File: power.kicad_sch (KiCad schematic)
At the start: 20 parts, among them IC3 CH224K, J5 USB_C_Receptacle_USB2.0, J6 Barrel_Jack, U13 TPD2EUSB30, U20 TPS5430DDA, U9 AMS1117-3.3

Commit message: Fix ERC warnings
See #28
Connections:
- no-connect marks 6 -> 7
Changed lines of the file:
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@@
+	)
+	(junction
+		(at 62.23 27.94)
+		(diameter 0)
+		(color 0 0 0 0)
 	)
 	(junction
@@
 	)
 	(no_connect
+		(at 151.13 35.56)
+	)
+	(no_connect
 		(at 40.64 173.99)
 	)
@@
 	(wire
 		(pts
+			(xy 54.61 25.4) (xy 54.61 27.94)
+		)
+		(stroke
+			(width 0)
+			(type default)
+		)
+	)
+	(wire
+		(pts
 			(xy 36.83 127) (xy 45.72 127)
 		)
@@
 	(wire
 		(pts
-			(xy 62.23 25.4) (xy 62.23 33.02)
+			(xy 62.23 25.4) (xy 62.23 27.94)
 		)
 		(stroke
@@
 	(wire
 		(pts
+			(xy 62.23 27.94) (xy 62.23 33.02)
+		)
+		(stroke
+			(width 0)
+			(type default)
+		)
+	)
+	(wire
+		(pts
 			(xy 77.47 168.91) (xy 83.82 168.91)
+		)
+		(stroke
+			(width 0)
+			(type default)
+		)
+	)
+	(wire
+		(pts
+			(xy 54.61 27.94) (xy 62.23 27.94)
 		)
 		(stroke
@@
 					(unit 1)
 				)
+			)
+		)
+	)
+	(symbol
+		(lib_id "power:PWR_FLAG")
+		(at 54.61 25.4 0)
+		(unit 1)
+		(exclude_from_sim no)
+		(in_bom yes)
+		(on_board yes)
+		(dnp no)
+		(fields_autoplaced yes)
+		(property "Reference" "#FLG09"
+			(at 54.61 23.495 0)
+			(effects
+				(font
+					(size 1.27 1.27)
+				)
+				(hide yes)
+			)
+		)
+		(property "Value" "PWR_FLAG"
+			(at 54.61 20.32 0)
+			(effects
+				(font
+					(size 1.27 1.27)
+				)
+			)
+		)
+		(property "Footprint" ""
+			(at 54.61 25.4 0)
+			(effects
+				(font
+					(size 1.27 1.27)
+				)
+				(hide yes)
+			)
+		)
+		(property "Datasheet" "~"
+			(at 54.61 25.4 0)
+			(effects
+				(font
+					(size 1.27 1.27)
+				)
+				(hide yes)
+			)
+		)
+		(property "Description" "Special symbol for telling ERC where power comes from"
+			(at 54.61 25.4 0)
+			(effects
+				(font
+					(size 1.27 1.27)
+				)
+				(hide yes)
+			)
+		)
+		(pin "1"
+		)
+		(instances
+			(project ""
+				(path "/b3c8a28b-9ce1-4002-b8e8-ef8cb73fe031/673a8a36-5ad4-4c13-9f11-024cf0bef494"
+					(reference "#FLG09")
+					(unit 1)
+				)

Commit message: Add missing rotation offset attribute
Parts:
- C39: JLCPCB Rotation Offset (none) -> 180
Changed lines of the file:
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@@
 			)
 		)
-		(property "LCSC alt" ""
+		(property "JLCPCB Rotation Offset" "180"
 			(at 97.79 172.72 0)
 			(effects

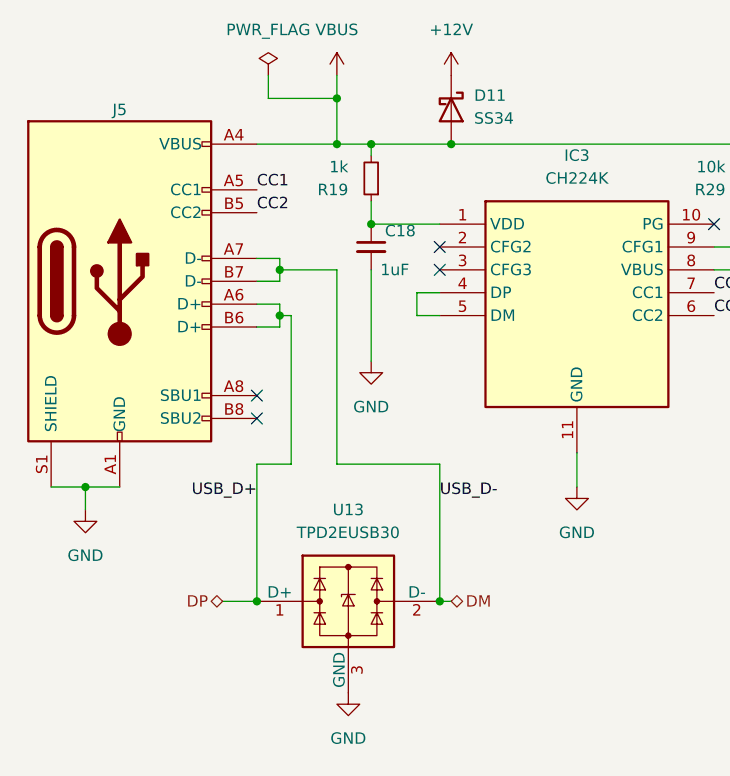
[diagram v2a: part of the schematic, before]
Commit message: Fix ERC errors
Closes #28
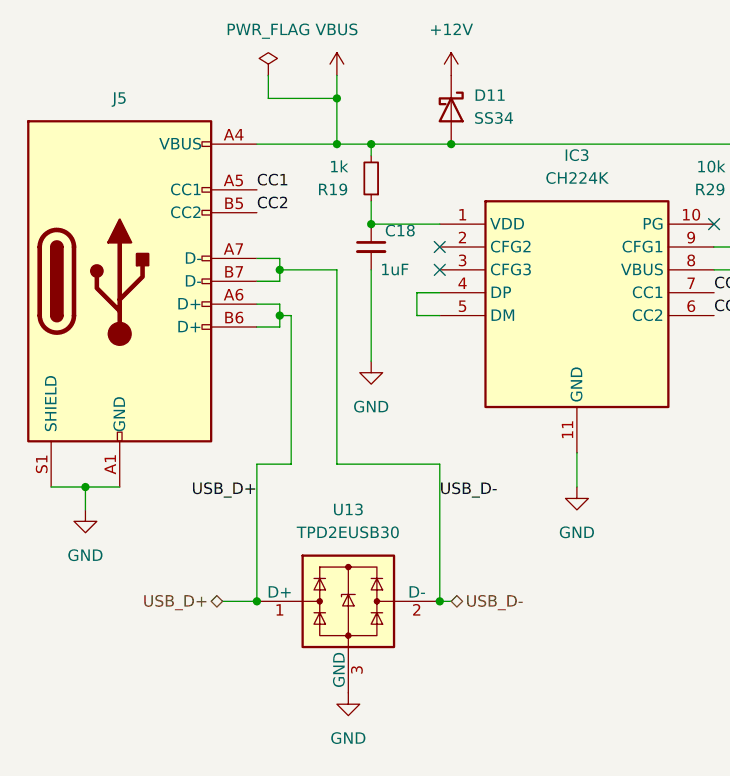
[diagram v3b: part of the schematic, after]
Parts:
- J5: symbol Connector:USB_C_Receptacle_USB2.0 -> Connector:USB_C_Receptacle_USB2.0_14P
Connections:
- net DM renamed USB_D-
- net DP renamed USB_D+
- no-connect marks 7 -> 5
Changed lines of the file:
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@@
 	)
 	(no_connect
-		(at 53.34 60.96)
-	)
-	(no_connect
 		(at 151.13 35.56)
 	)
@@
 	)
 	(no_connect
-		(at 53.34 63.5)
-	)
-	(no_connect
 		(at 73.66 46.99)
 	)
@@
 		)
 	)
-	(hierarchical_label "DM"
+	(hierarchical_label "USB_D-"
 		(shape bidirectional)
 		(at 74.93 83.82 0)
@@
 		)
 	)
-	(hierarchical_label "DP"
+	(hierarchical_label "USB_D+"
 		(shape bidirectional)
 		(at 49.53 83.82 180)
@@
 	)
 	(symbol
-		(lib_id "Connector:USB_C_Receptacle_USB2.0")
+		(lib_id "Connector:USB_C_Receptacle_USB2.0_14P")
 		(at 38.1 48.26 0)
 		(unit 1)
@@
 		(fields_autoplaced yes)
 		(property "Reference" "J5"
-			(at 38.1 29.21 0)
+			(at 38.1 27.94 0)
 			(effects
 				(font
@@
 		(pin "A7"
 		)
-		(pin "A8"
-		)
 		(pin "A9"
 		)
@@
 		(pin "B7"
 		)
-		(pin "B8"
-		)
 		(pin "B9"

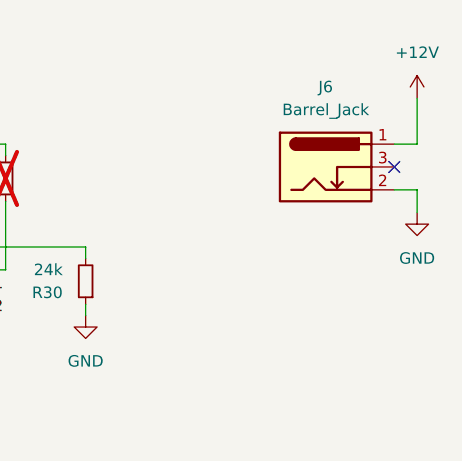
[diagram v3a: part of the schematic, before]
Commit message: Connect GND on DC barrel jack
Closes #35
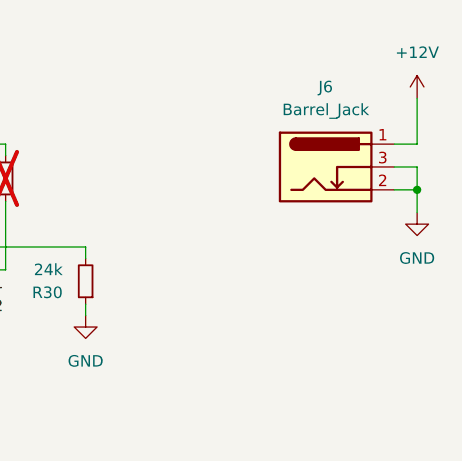
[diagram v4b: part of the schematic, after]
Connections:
- net GND: now also J6.3
- no-connect marks 5 -> 4
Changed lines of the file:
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@@
+	)
+	(junction
+		(at 153.67 38.1)
+		(diameter 0)
+		(color 0 0 0 0)
 	)
 	(junction
@@
 	)
 	(no_connect
-		(at 151.13 35.56)
-	)
-	(no_connect
 		(at 40.64 173.99)
 	)
@@
 	(wire
 		(pts
+			(xy 151.13 35.56) (xy 153.67 35.56)
+		)
+		(stroke
+			(width 0)
+			(type default)
+		)
+	)
+	(wire
+		(pts
 			(xy 66.04 33.02) (xy 66.04 34.29)
 		)
@@
 		)
 		(stroke
+			(width 0)
+			(type default)
+		)
+	)
+	(wire
+		(pts
+			(xy 153.67 35.56) (xy 153.67 38.1)
+		)
+		(stroke

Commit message: Update footprint for U13
Closes #33
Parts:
- U13: footprint Package_TO_SOT_SMD:Texas_DRT-3 -> Package_TO_SOT_SMD:SOT-723
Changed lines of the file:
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@@
 			)
 		)
-		(property "Footprint" "Package_TO_SOT_SMD:Texas_DRT-3"
+		(property "Footprint" "Package_TO_SOT_SMD:SOT-723"
 			(at 44.45 91.44 0)
 			(effects
@@
 			)
 		)
-		(property "Datasheet" "http://www.ti.com/lit/ds/symlink/tpd2eusb30a.pdf"
+		(property "Datasheet" "https://www.lcsc.com/datasheet/lcsc_datasheet_2411121100_TECH-PUBLIC-TPD2EUSB30DRTR-TP_C2844720.pdf"
 			(at 63.5 83.82 0)
 			(effects

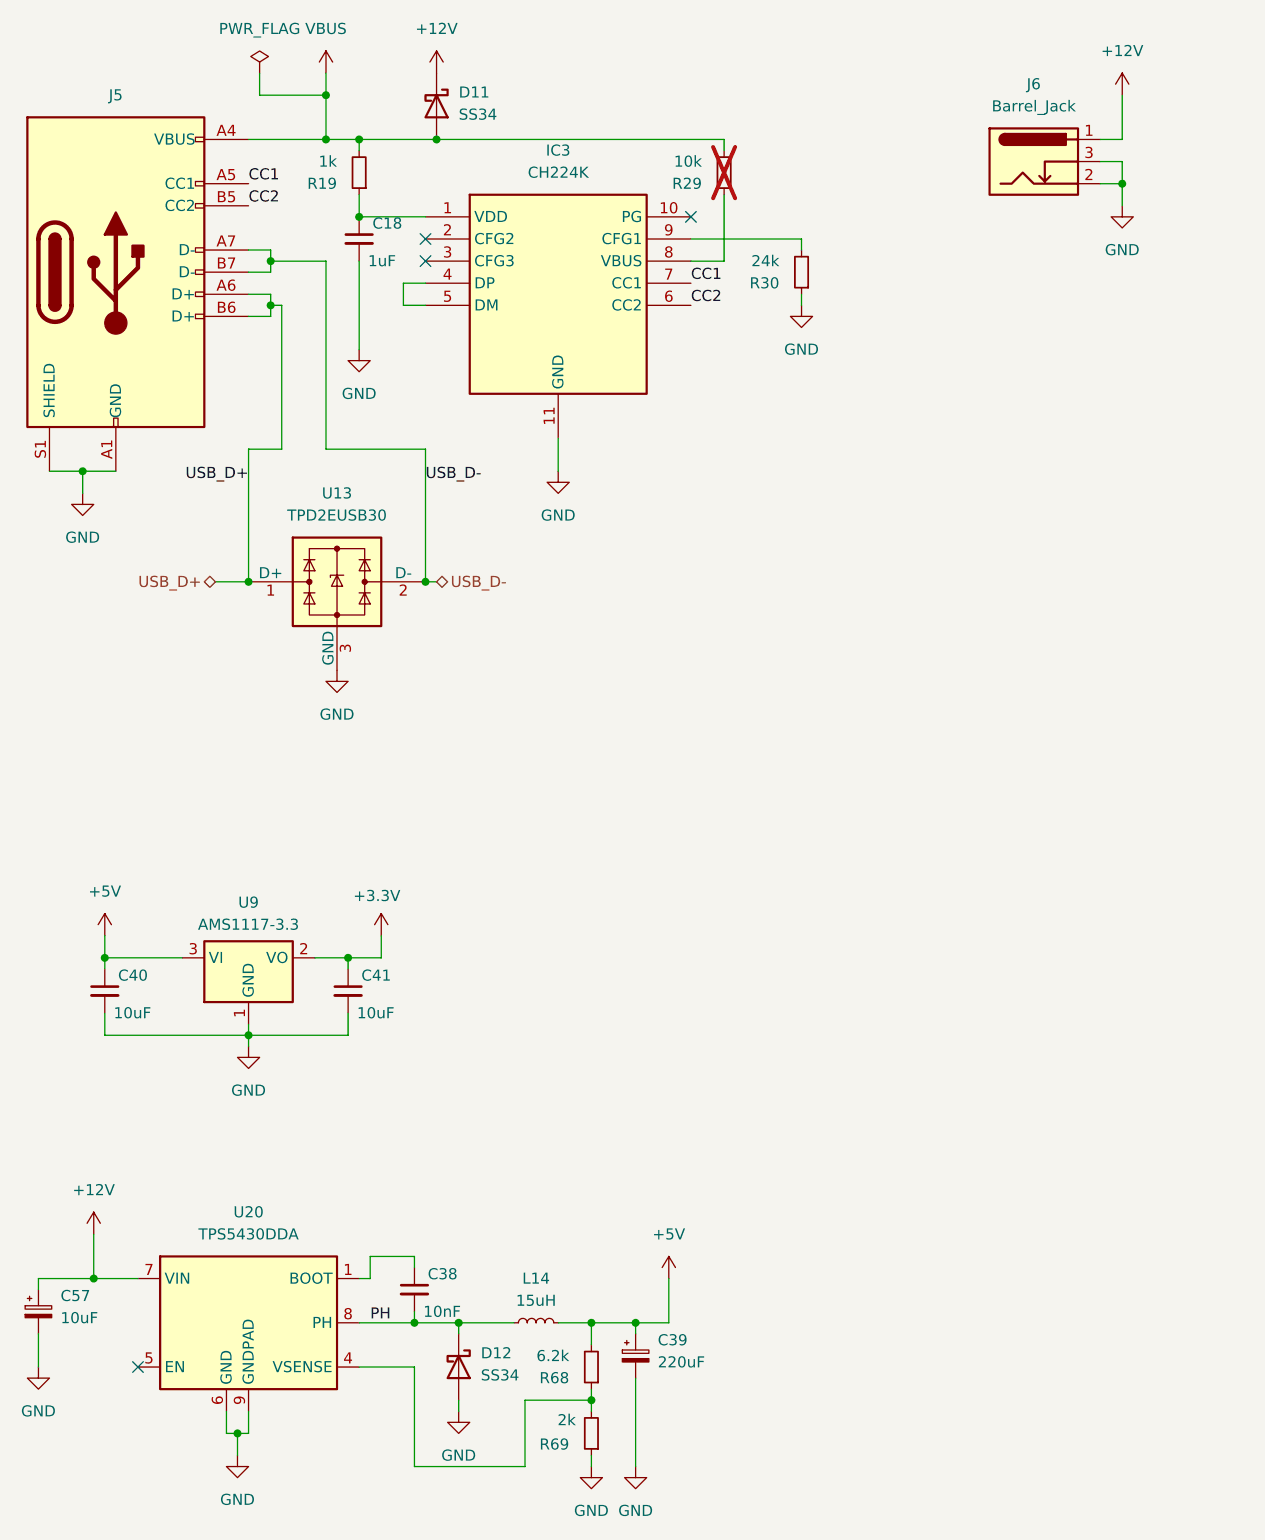
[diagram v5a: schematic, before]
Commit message: Add testpoints
Closes #47
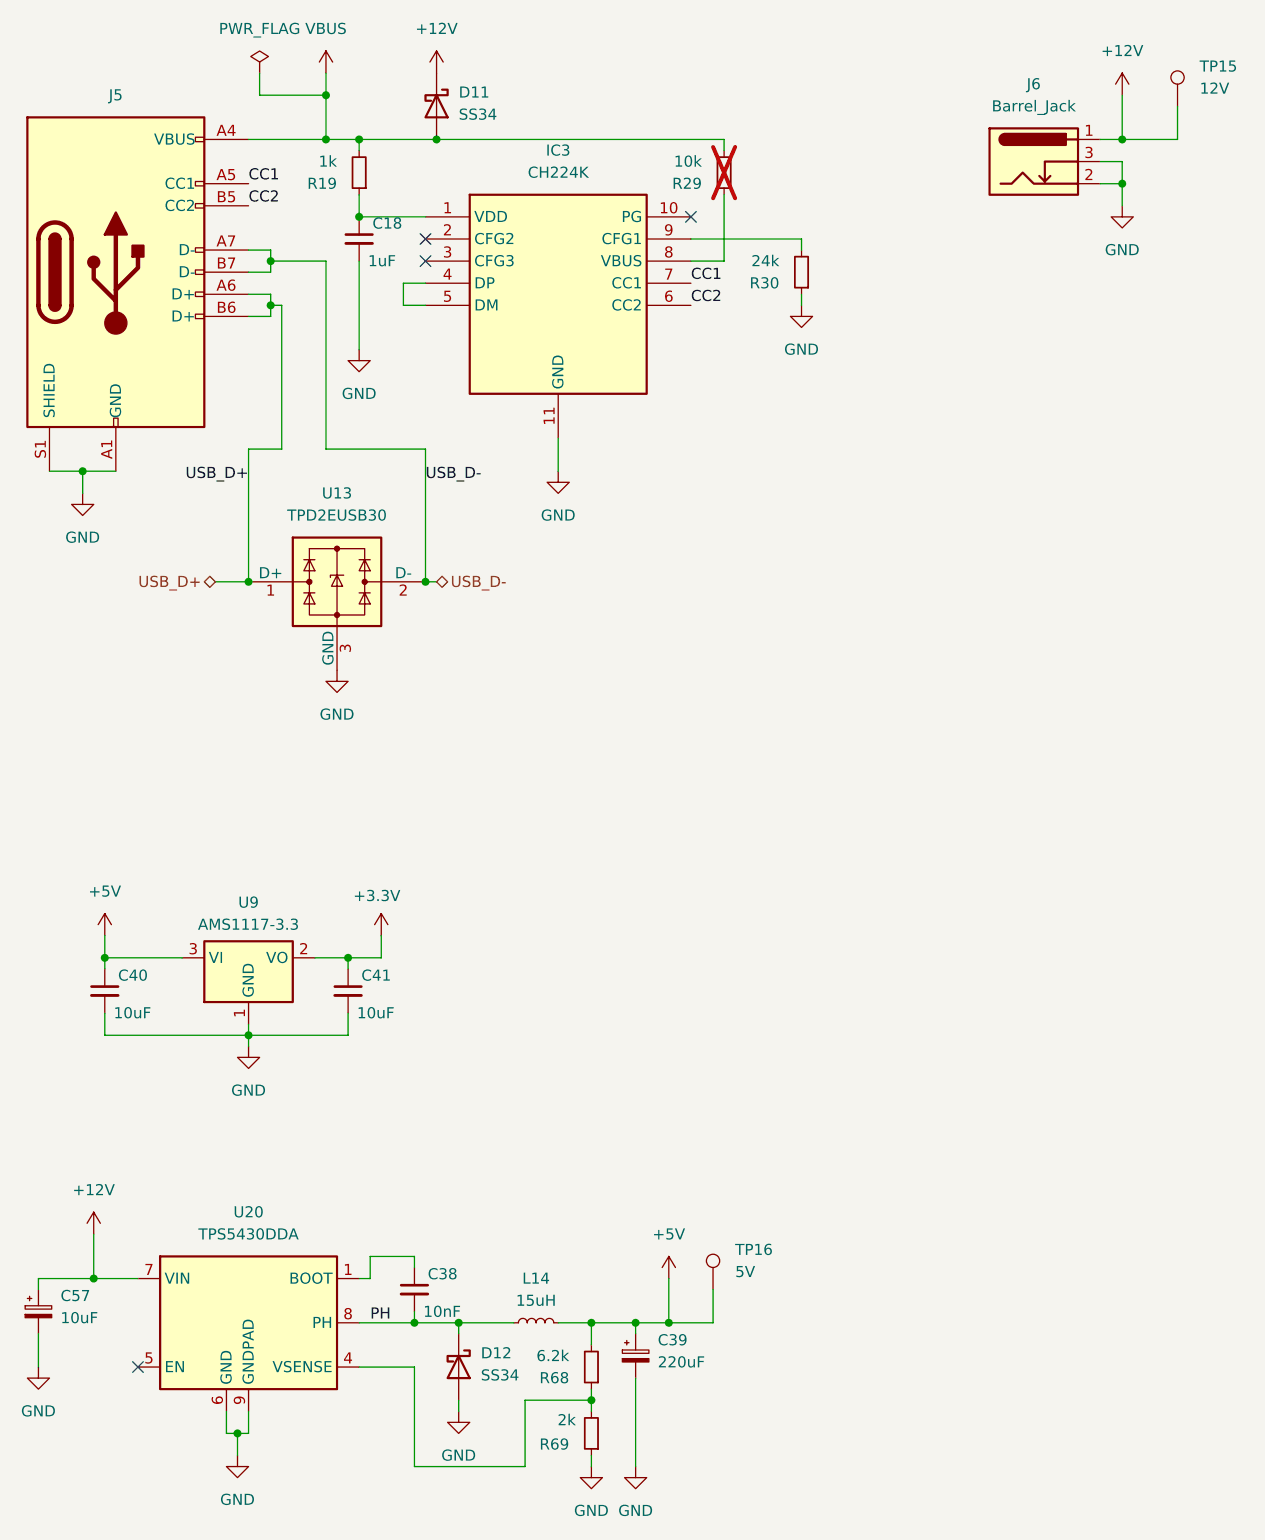
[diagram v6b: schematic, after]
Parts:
- added TP15: 12V, TestPoint:TestPoint_Pad_D1.5mm, symbol Connector:TestPoint
- added TP16: 5V, TestPoint:TestPoint_Pad_D1.5mm, symbol Connector:TestPoint
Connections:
- net +12V: now also TP15.1
- net +5V: now also TP16.1
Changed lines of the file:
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@@
 	)
 	(junction
+		(at 153.67 33.02)
+		(diameter 0)
+		(color 0 0 0 0)
+	)
+	(junction
 		(at 52.07 181.61)
 		(diameter 0)
@@
 	)
 	(junction
+		(at 101.6 168.91)
+		(diameter 0)
+		(color 0 0 0 0)
+	)
+	(junction
 		(at 92.71 177.8)
 		(diameter 0)
@@
 	(wire
 		(pts
+			(xy 160.02 29.21) (xy 160.02 33.02)
+		)
+		(stroke
+			(width 0)
+			(type default)
+		)
+	)
+	(wire
+		(pts
 			(xy 92.71 168.91) (xy 97.79 168.91)
 		)
@@
 	(wire
 		(pts
+			(xy 106.68 165.1) (xy 106.68 168.91)
+		)
+		(stroke
+			(width 0)
+			(type default)
+		)
+	)
+	(wire
+		(pts
 			(xy 73.66 49.53) (xy 71.12 49.53)
 		)
@@
 	(wire
 		(pts
+			(xy 106.68 168.91) (xy 101.6 168.91)
+		)
+		(stroke
+			(width 0)
+			(type default)
+		)
+	)
+	(wire
+		(pts
 			(xy 35.56 163.83) (xy 40.64 163.83)
 		)
@@
 	(wire
 		(pts
+			(xy 160.02 33.02) (xy 153.67 33.02)
+		)
+		(stroke
+			(width 0)
+			(type default)
+		)
+	)
+	(wire
+		(pts
 			(xy 74.93 33.02) (xy 107.95 33.02)
 		)
@@
 	)
 	(symbol
+		(lib_id "Connector:TestPoint")
+		(at 106.68 165.1 0)
+		(unit 1)
+		(exclude_from_sim no)
+		(in_bom no)
+		(on_board yes)
+		(dnp no)
+		(fields_autoplaced yes)
+		(property "Reference" "TP16"
+			(at 109.22 160.5279 0)
+			(effects
+				(font
+					(size 1.27 1.27)
+				)
+				(justify left)
+			)
+		)
+		(property "Value" "5V"
+			(at 109.22 163.0679 0)
+			(effects
+				(font
+					(size 1.27 1.27)
+				)
+				(justify left)
+			)
+		)
+		(property "Footprint" "TestPoint:TestPoint_Pad_D1.5mm"
+			(at 111.76 165.1 0)
+			(effects
+				(font
+					(size 1.27 1.27)
+				)
+				(hide yes)
+			)
+		)
+		(property "Datasheet" "~"
+			(at 111.76 165.1 0)
+			(effects
+				(font
+					(size 1.27 1.27)
+				)
+				(hide yes)
+			)
+		)
+		(property "Description" "test point"
+			(at 106.68 165.1 0)
+			(effects
+				(font
+					(size 1.27 1.27)
+				)
+				(hide yes)
+			)
+		)
+		(pin "1"
+		)
+		(instances
+			(project ""
+				(path "/b3c8a28b-9ce1-4002-b8e8-ef8cb73fe031/673a8a36-5ad4-4c13-9f11-024cf0bef494"
+					(reference "TP16")
+					(unit 1)
+				)
+			)
+		)
+	)
+	(symbol
 		(lib_id "Connector:USB_C_Receptacle_USB2.0_14P")
 		(at 38.1 48.26 0)
@@
 					(unit 1)
 				)
+			)
+		)
+	)
+	(symbol
+		(lib_id "Connector:TestPoint")
+		(at 160.02 29.21 0)
+		(unit 1)
+		(exclude_from_sim no)
+		(in_bom no)
+		(on_board yes)
+		(dnp no)
+		(fields_autoplaced yes)
+		(property "Reference" "TP15"
+			(at 162.56 24.6379 0)
+			(effects
+				(font
+					(size 1.27 1.27)
+				)
+				(justify left)
+			)
+		)
+		(property "Value" "12V"
+			(at 162.56 27.1779 0)
+			(effects
+				(font
+					(size 1.27 1.27)
+				)
+				(justify left)
+			)
+		)
+		(property "Footprint" "TestPoint:TestPoint_Pad_D1.5mm"
+			(at 165.1 29.21 0)
+			(effects
+				(font
+					(size 1.27 1.27)
+				)
+				(hide yes)
+			)
+		)
+		(property "Datasheet" "~"
+			(at 165.1 29.21 0)
+			(effects
+				(font
+					(size 1.27 1.27)
+				)
+				(hide yes)
+			)
+		)
+		(property "Description" "test point"
+			(at 160.02 29.21 0)
+			(effects
+				(font
+					(size 1.27 1.27)
+				)
+				(hide yes)
+			)
+		)
+		(pin "1"
+		)
+		(instances
+			(project ""
+				(path "/b3c8a28b-9ce1-4002-b8e8-ef8cb73fe031/673a8a36-5ad4-4c13-9f11-024cf0bef494"
+					(reference "TP15")
+					(unit 1)
+				)

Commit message: Update manufacturing positions and rotations of parts
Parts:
- J6: JLCPCB Position Offset (none) -> -0.1,0.5
- U13: JLCPCB Rotation Offset (none) -> 180
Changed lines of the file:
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@@
+			)
+		)
+		(property "JLCPCB Rotation Offset" "180"
+			(at 63.5 83.82 0)
+			(effects
+				(font
+					(size 1.27 1.27)
+				)
+				(hide yes)
 			)
 		)
@@
 			(at 143.51 35.56 0)
 			(effects
+				(font
+					(size 1.27 1.27)
+				)
+				(hide yes)
+			)
+		)
+		(property "JLCPCB Position Offset" "-0.1,0.5"
+			(at 143.51 35.56 0)
+			(effects
